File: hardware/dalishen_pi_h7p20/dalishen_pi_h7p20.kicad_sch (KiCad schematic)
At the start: 99 parts, among them J1 Conn_02x05_Odd_Even, J6 5V, J7 OV5640, J9 D500C930SV0, SW1 SW_Push, SW2 SW_Push, SW3 SW_DIP_x03, SW4 SW_Push, SW5 SW_Push, U3 H7P20N0L128-M3H1, U4 SY7201ABC, U5 XC6206-2.8, U7 P25Q64SH-SSH-IR, U8 XC6206-1.5, X1 NC

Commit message: [dalishen_pi_h7p20] 68013替换为双USB3343
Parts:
- removed C2: NC, Capacitor_SMD:C_0402_1005Metric, symbol Device:C
- removed CY_J1, CY_J2: Conn_02x10_Odd_Even, Connector_PinSocket_2.54mm:PinSocket_2x10_P2.54mm_Vertical, symbol Connector_Generic:Conn_02x10_Odd_Even
- removed J6: 5V, Connector_PinSocket_2.54mm:PinSocket_1x01_P2.54mm_Vertical, symbol Connector_Generic:Conn_01x01
- removed JP1: SolderJumper_2_Open, Jumper:SolderJumper-2_P1.3mm_Open_RoundedPad1.0x1.5mm, symbol Jumper:SolderJumper_2_Open
- removed R16: 2.49k, Resistor_SMD:R_0402_1005Metric, symbol Device:R
- removed R7: NC, Resistor_SMD:R_0402_1005Metric, symbol Device:R
- removed R8: 33, Resistor_SMD:R_0402_1005Metric, symbol Device:R
- removed X1: NC, vllogic:OSC_3225, symbol Oscillator:XO32
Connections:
- net LED_PWM: no longer U3.8 (IO17_8)
- net USB334x_SP1_D4: now reaches U3.6 (IO13_PCLK_8)
- net CY_FD_0 renamed USB334x_SP1_STP
- net CY_FD_1 renamed USB334x_SP1_DIR
- net CY_FD_10 renamed USB334x_SP2_CLK
- net CY_FD_11 renamed USB334x_SP1_26M
- net CY_FD_12 renamed USB334x_SP1_NXT
- net CY_FD_13 renamed USB334x_SP1_CLK
- net CY_FD_14 renamed USB334x_SP1_D0
- net CY_FD_15 renamed USB334x_SP1_D1
- net CY_FD_2 renamed USB334x_SP1_D7
- net CY_FD_3 renamed USB334x_SP1_D6
- net CY_FD_4 renamed USB334x_SP2_26M
- net CY_FD_5 renamed USB334x_SP2_NXT
- net CY_FD_6 renamed USB334x_SP2_STP
- net CY_FD_7 renamed USB334x_SP2_DIR
- net CY_FD_8 renamed USB334x_SP2_D1
- net CY_FD_9 renamed USB334x_SP2_D0
- net CY_FLAGB renamed USB334x_SP2_D7
- net CY_IFCLK renamed USB334x_SP1_D3
- net CY_PA0 renamed USB334x_SP2_D5
- net CY_PA1 renamed USB334x_SP2_D4
- net CY_PA3 renamed USB334x_SP2_D3
- net CY_PKTEND renamed USB334x_SP2_D2
- net CY_SLRD renamed USB334x_SP2_D6
- net CY_SLWR renamed USB334x_SP1_D2
- new net USB334x_SP1_D5: U3.8 (IO17_8)
- no-connect marks 16 -> 12
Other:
- added sheet USB334x_SP1 (USB334x_SP.kicad_sch)
- added sheet USB334x_SP2 (USB334x_SP.kicad_sch)
- sheet USB334x ports: added none; removed USB20_DM_CMP1, USB20_DM_CMP2, USB20_DM_CMP3, USB20_DP_CMP1, USB20_DP_CMP2, USB20_DP_CMP3
- note removed: "EZ-USB CY7C68013A板 对接口（顶对顶） 若68013板已焊排针，本板需焊双排母对接"
- note removed: "PD3 PD1 PA7 PA5 PA3 PA1 CTL2 CTL0 PB6 PB4"
- note removed: "PD4 PD2 PD0 PA6 PA4 PA2 PA0 CTL1 PB7 PB5"
- note removed: "PD5 PD7 CLK RDY0 GND GND SCL PB0 PB2 GND"
- note removed: "PD6 GND GND RDY1 VCC IFCLK SDA PB1 PB3 VCC"
- note removed: "注：JP1短接后可对外输出3.3V。对接EZ-USB板时不要短接。"
- moved on the sheet: C10, C11, C16, C17, C18, C19, C20, C21, C22, C23, C24, C38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

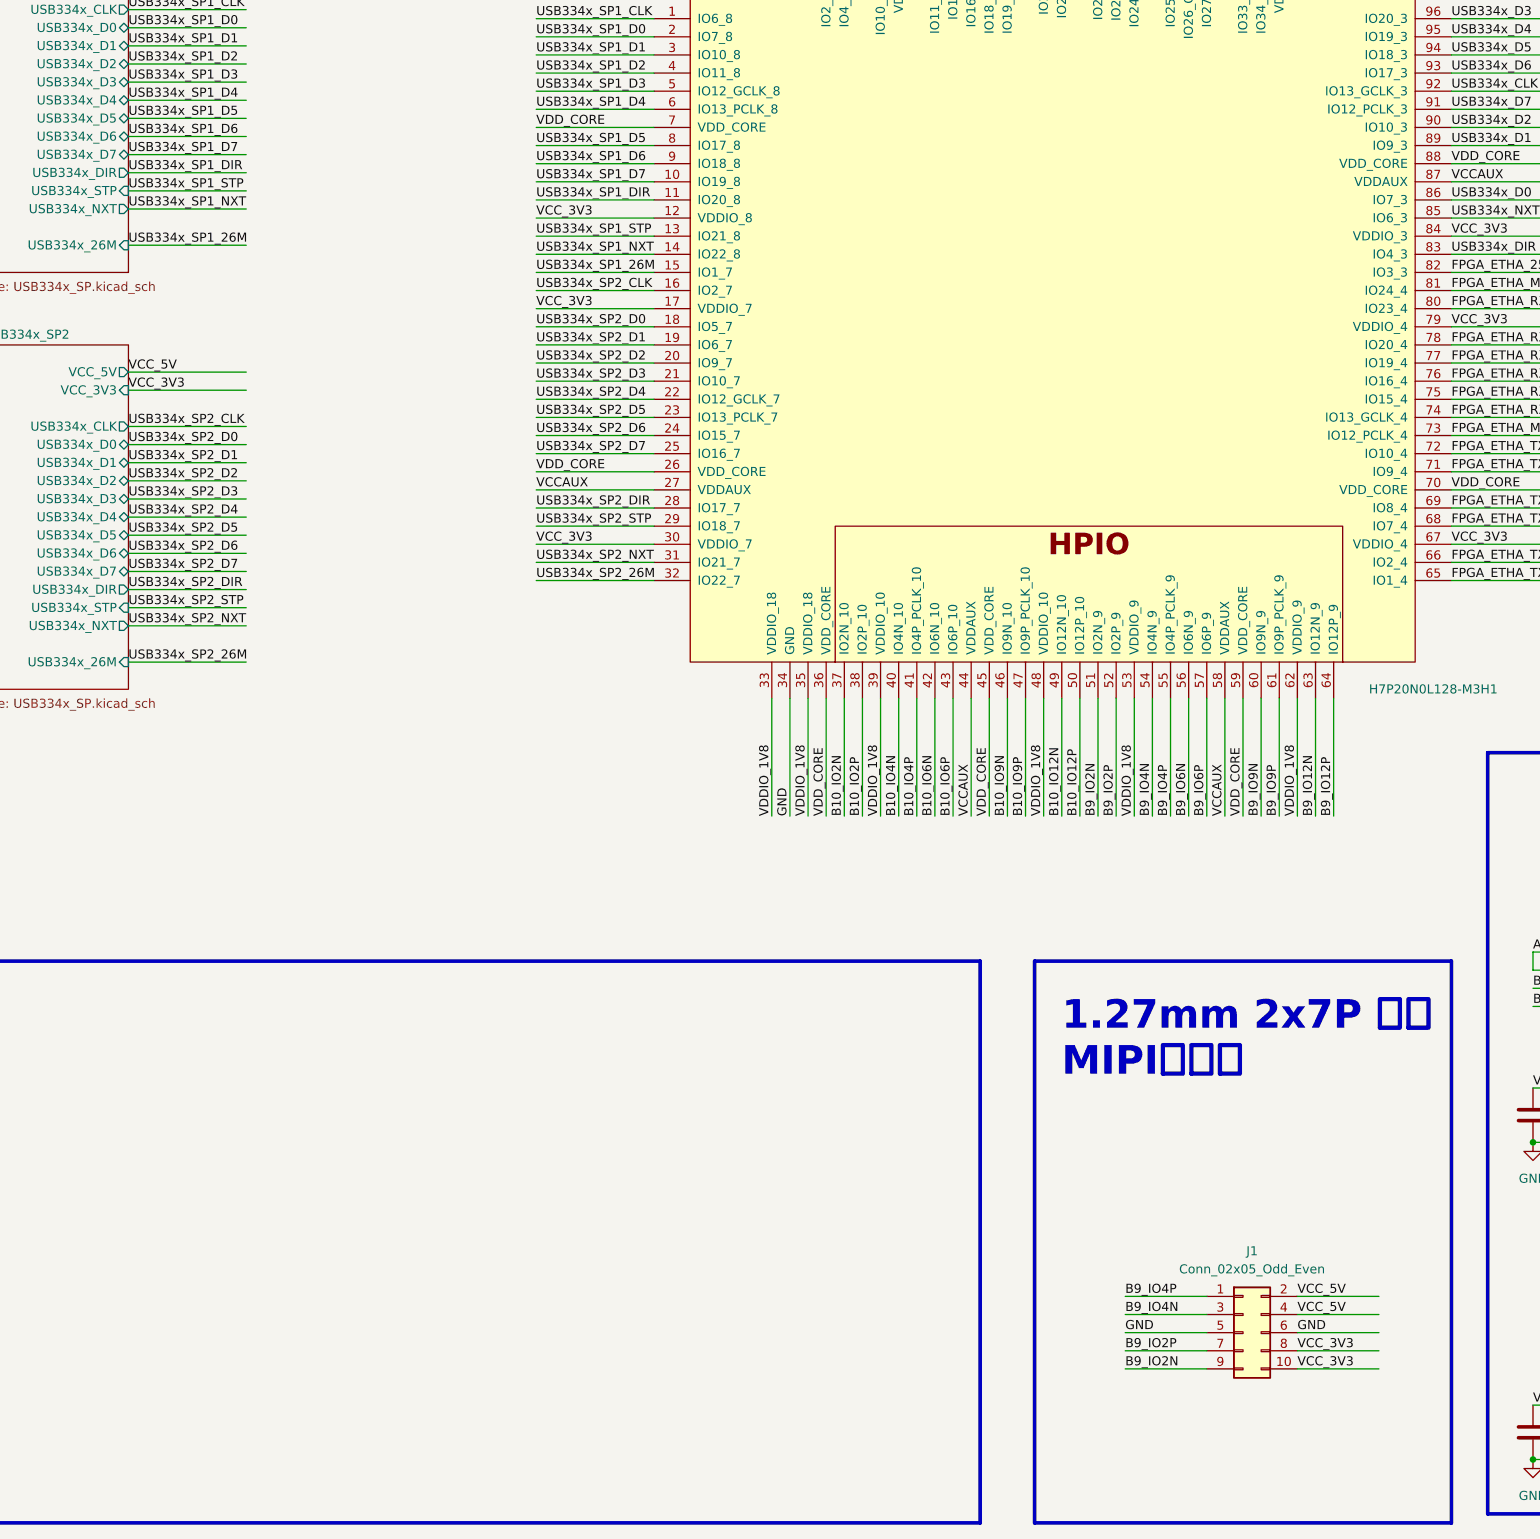
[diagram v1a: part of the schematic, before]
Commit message: [dalishen_pi_h7p20] 增加I2C小屏，增加两个测试IO
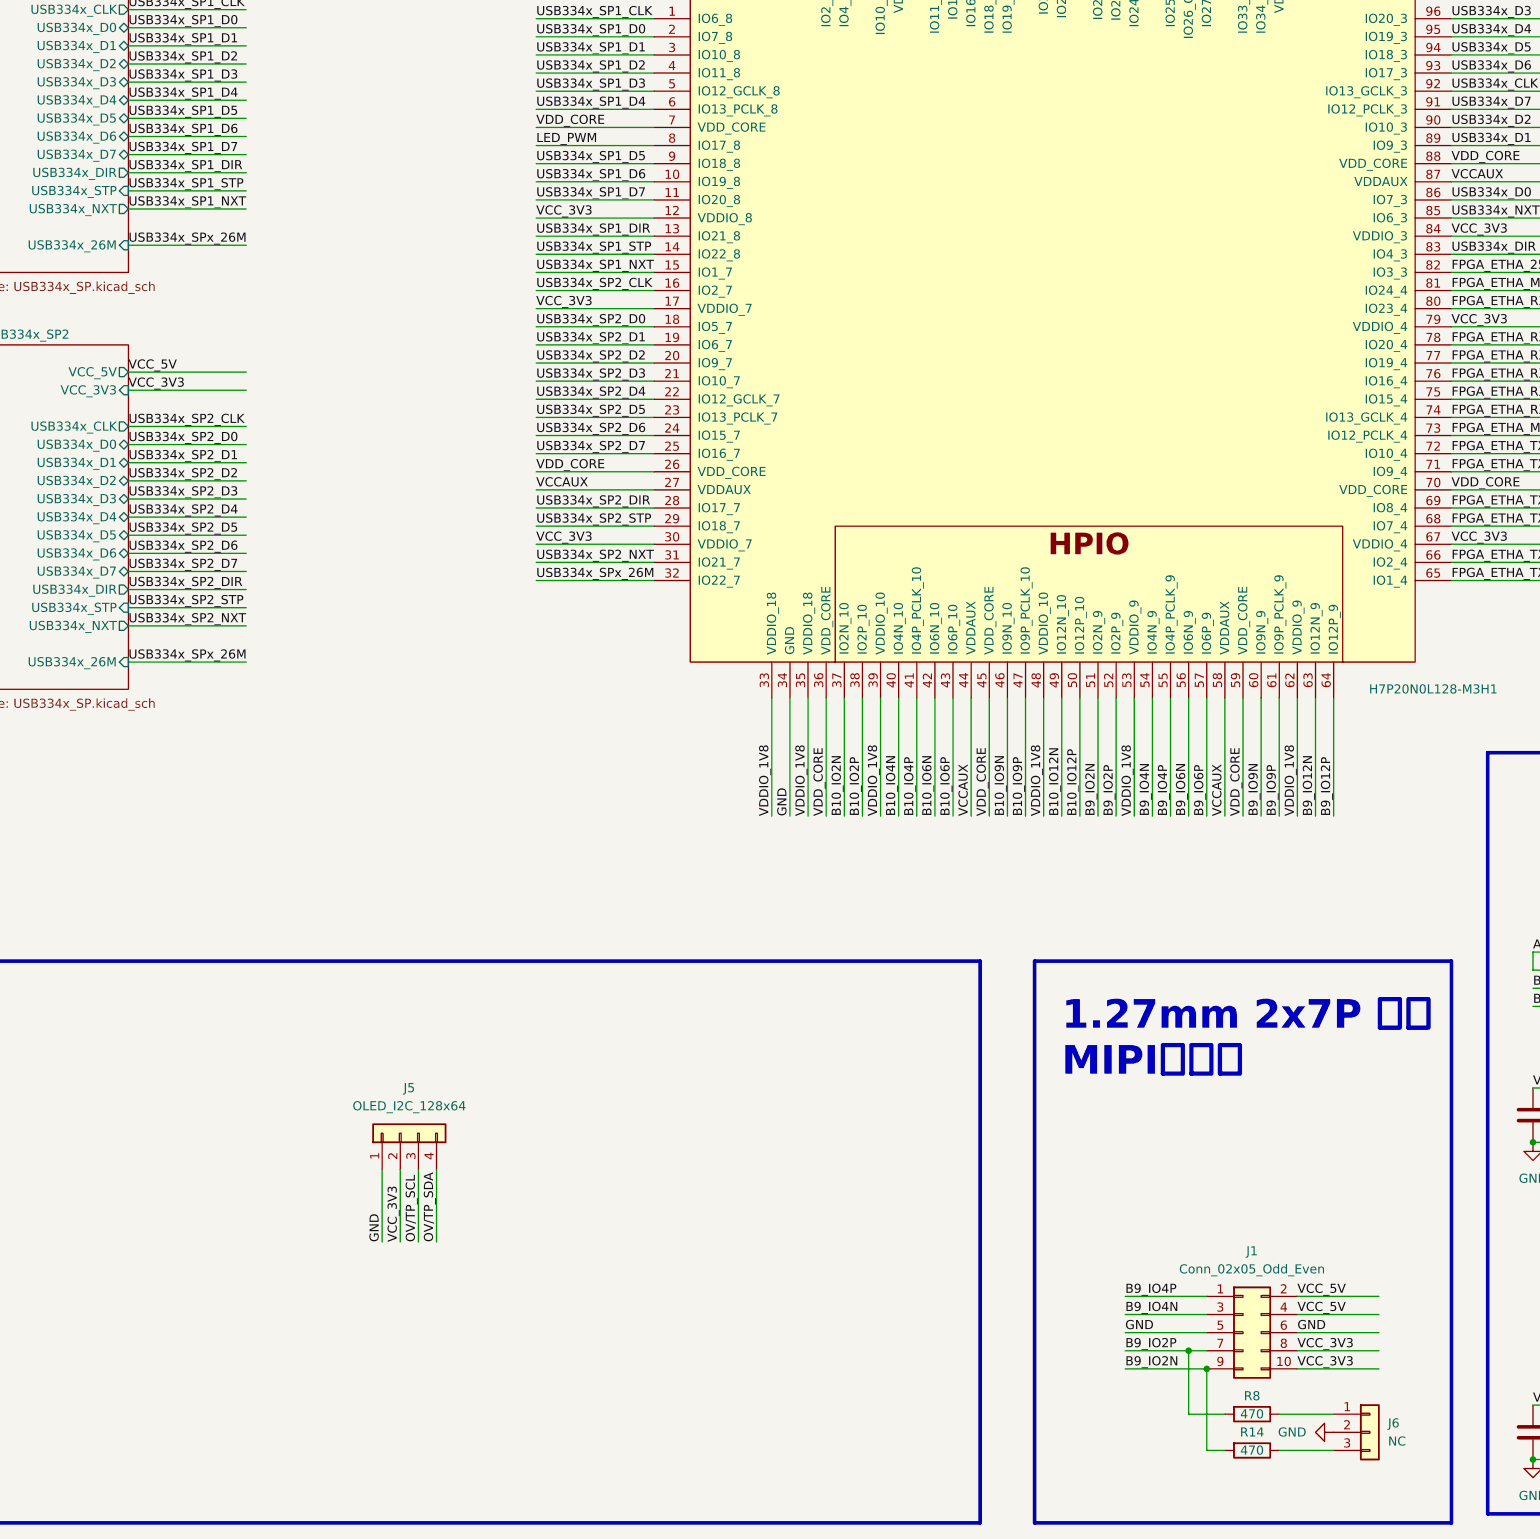
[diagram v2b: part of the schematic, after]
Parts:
- added J5: OLED_I2C_128x64, symbol Connector_Generic:Conn_01x04
- added J6: NC, symbol Connector_Generic:Conn_01x03
- added R14, R8: 470, Resistor_SMD:R_0402_1005Metric, symbol Device:R
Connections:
- net USB334x_SP1_26M is gone; now on net USB334x_SP1_NXT: U3.15 (IO1_7)
- net B9_IO2N: now also R14.2
- net B9_IO2P: now also R8.2
- net GND: now also J5.1 (Pin_1), J6.2 (Pin_2)
- net LED_PWM: now also U3.8 (IO17_8)
- net OV/TP_SCL: now also J5.3 (Pin_3)
- net OV/TP_SDA: now also J5.4 (Pin_4)
- net USB334x_SP1_D5: now also U3.9 (IO18_8); no longer U3.8 (IO17_8)
- net USB334x_SP1_D6: now also U3.10 (IO19_8); no longer U3.9 (IO18_8)
- net USB334x_SP1_D7: now also U3.11 (IO20_8); no longer U3.10 (IO19_8)
- net USB334x_SP1_DIR: now also U3.13 (IO21_8); no longer U3.11 (IO20_8)
- net USB334x_SP1_NXT: no longer U3.14 (IO22_8)
- net USB334x_SP1_STP: now also U3.14 (IO22_8); no longer U3.13 (IO21_8)
- net VCC_3V3: now also J5.2 (Pin_2)
- net USB334x_SP2_26M renamed USB334x_SPx_26M
- new net: J6.1 (Pin_1), R8.1
- new net: J6.3 (Pin_3), R14.1

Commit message: [dalishen_pi_h7p20] Backup
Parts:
- added FID1, FID2, FID3: Fiducial, Fiducial:Fiducial_1mm_Mask2mm, symbol Mechanical:Fiducial
- added R10, R24: 33, Resistor_SMD:R_0402_1005Metric, symbol Device:R
- J5: footprint (none) -> Connector_PinSocket_2.54mm:PinSocket_1x04_P2.54mm_Vertical
- J6: footprint (none) -> Connector_PinHeader_2.54mm:PinHeader_1x03_P2.54mm_Vertical
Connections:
- net USB334x_SPx_26M: now also R10.1, R24.1
- new net USB334x_SP1/USB334x_26M: R24.2
- new net USB334x_SP2/USB334x_26M: R10.2

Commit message: [dalishen_pi_h7p20] Backup
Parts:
- J6: footprint Connector_PinHeader_2.54mm:PinHeader_1x03_P2.54mm_Vertical -> Connector_PinHeader_2.54mm:PinHeader_1x03_P2.54mm_Horizontal
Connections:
- net KEY0 is gone; now on net KEY1: SW1.1, U3.126 (IO3_8)
- net KEY1: no longer SW4.1, U3.104 (IO27_GCLK_2)
- net KEY2: now also SW4.1, U3.104 (IO27_GCLK_2); no longer SW5.1, U3.102 (IO33_MISO3_2)
- net USB334x_SP1_CLK: now also U3.5 (IO12_GCLK_8); no longer U3.1 (IO6_8)
- net USB334x_SP1_D0: now also U3.3 (IO10_8); no longer U3.2 (IO7_8)
- net USB334x_SP1_D1: now also U3.2 (IO7_8); no longer U3.3 (IO10_8)
- net USB334x_SP1_D2: now also U3.1 (IO6_8); no longer U3.4 (IO11_8)
- net USB334x_SP1_D3: now also U3.13 (IO21_8); no longer U3.5 (IO12_GCLK_8)
- net USB334x_SP1_D4: now also U3.11 (IO20_8); no longer U3.6 (IO13_PCLK_8)
- net USB334x_SP1_D5: now also U3.10 (IO19_8); no longer U3.9 (IO18_8)
- net USB334x_SP1_D6: now also U3.9 (IO18_8); no longer U3.10 (IO19_8)
- net USB334x_SP1_D7: now also U3.6 (IO13_PCLK_8); no longer U3.11 (IO20_8)
- net USB334x_SP1_DIR: now also U3.14 (IO22_8); no longer U3.13 (IO21_8)
- net USB334x_SP1_NXT: now also U3.4 (IO11_8); no longer U3.15 (IO1_7)
- net USB334x_SP1_STP: now also U3.15 (IO1_7); no longer U3.14 (IO22_8)
- net USB334x_SP2_CLK: now also U3.22 (IO12_GCLK_7); no longer U3.16 (IO2_7)
- net USB334x_SP2_D0: now also U3.20 (IO9_7); no longer U3.18 (IO5_7)
- net USB334x_SP2_D2: now also U3.18 (IO5_7); no longer U3.20 (IO9_7)
- net USB334x_SP2_D3: now also U3.29 (IO18_7); no longer U3.21 (IO10_7)
- net USB334x_SP2_D4: now also U3.28 (IO17_7); no longer U3.22 (IO12_GCLK_7)
- net USB334x_SP2_D5: now also U3.25 (IO16_7); no longer U3.23 (IO13_PCLK_7)
- net USB334x_SP2_D7: now also U3.23 (IO13_PCLK_7); no longer U3.25 (IO16_7)
- net USB334x_SP2_DIR: now also U3.31 (IO21_7); no longer U3.28 (IO17_7)
- net USB334x_SP2_NXT: now also U3.21 (IO10_7); no longer U3.31 (IO21_7)
- net USB334x_SP2_STP: now also U3.32 (IO22_7); no longer U3.29 (IO18_7)
- net USB334x_SPx_26M: now also U3.16 (IO2_7); no longer U3.32 (IO22_7)
- new net KEY3: SW5.1, U3.102 (IO33_MISO3_2)
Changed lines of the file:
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@@
 		)
 	)
-	(label "KEY1"
+	(label "KEY2"
 		(at 189.23 54.61 90)
 		(effects
@@
 	)
 	(label "USB334x_SP2_D4"
-		(at 95.25 124.46 0)
+		(at 95.25 139.7 0)
 		(effects
 			(font
@@
 	)
 	(label "USB334x_SP1_D0"
-		(at 95.25 73.66 0)
+		(at 95.25 76.2 0)
 		(effects
 			(font
@@
 	)
 	(label "USB334x_SP1_D6"
-		(at 95.25 93.98 0)
+		(at 95.25 91.44 0)
 		(effects
 			(font
@@
 	)
 	(label "USB334x_SP1_D5"
-		(at 95.25 91.44 0)
+		(at 95.25 93.98 0)
 		(effects
 			(font
@@
 	)
 	(label "USB334x_SP1_D7"
-		(at 95.25 96.52 0)
+		(at 95.25 83.82 0)
 		(effects
 			(font
@@
 	)
 	(label "USB334x_SP2_D5"
-		(at 95.25 127 0)
+		(at 95.25 132.08 0)
 		(effects
 			(font
@@
 	)
 	(label "USB334x_SP1_D1"
-		(at 95.25 76.2 0)
+		(at 95.25 73.66 0)
 		(effects
 			(font
@@
 	)
 	(label "USB334x_SP1_D4"
-		(at 95.25 83.82 0)
+		(at 95.25 96.52 0)
 		(effects
 			(font
@@
 		)
 	)
-	(label "KEY0"
+	(label "KEY1"
 		(at 133.35 54.61 90)
 		(effects
@@
 		)
 	)
-	(label "KEY2"
+	(label "KEY3"
 		(at 264.16 88.9 0)
 		(effects
@@
 		)
 	)
-	(label "KEY2"
+	(label "KEY3"
 		(at 194.31 54.61 90)
 		(effects
@@
 	)
 	(label "USB334x_SP1_NXT"
-		(at 95.25 106.68 0)
+		(at 95.25 78.74 0)
 		(effects
 			(font
@@
 	)
 	(label "USB334x_SP1_STP"
-		(at 95.25 104.14 0)
+		(at 95.25 106.68 0)
 		(effects
 			(font
@@
 		)
 	)
-	(label "KEY1"
+	(label "KEY2"
 		(at 264.16 83.82 0)
 		(effects
@@
 	)
 	(label "USB334x_SP1_D2"
-		(at 95.25 78.74 0)
+		(at 95.25 71.12 0)
 		(effects
 			(font
@@
 	)
 	(label "USB334x_SP2_D0"
-		(at 95.25 114.3 0)
+		(at 95.25 119.38 0)
 		(effects
 			(font
@@
 	)
 	(label "USB334x_SP2_D3"
-		(at 95.25 121.92 0)
+		(at 95.25 142.24 0)
 		(effects
 			(font
@@
 	)
 	(label "USB334x_SP2_D2"
-		(at 95.25 119.38 0)
+		(at 95.25 114.3 0)
 		(effects
 			(font
@@
 	)
 	(label "USB334x_SP2_DIR"
-		(at 95.25 139.7 0)
+		(at 95.25 147.32 0)
 		(effects
 			(font
@@
 	)
 	(label "USB334x_SP1_CLK"
-		(at 95.25 71.12 0)
+		(at 95.25 81.28 0)
 		(effects
 			(font
@@
 	)
 	(label "USB334x_SP2_CLK"
-		(at 95.25 109.22 0)
+		(at 95.25 124.46 0)
 		(effects
 			(font
@@
 	)
 	(label "USB334x_SP2_D7"
-		(at 95.25 132.08 0)
+		(at 95.25 127 0)
 		(effects
 			(font
@@
 		)
 	)
-	(label "KEY0"
+	(label "KEY1"
 		(at 264.16 78.74 0)
 		(effects
@@
 	)
 	(label "USB334x_SP1_D3"
-		(at 95.25 81.28 0)
+		(at 95.25 101.6 0)
 		(effects
 			(font
@@
 	)
 	(label "USB334x_SP2_STP"
-		(at 95.25 142.24 0)
+		(at 95.25 149.86 0)
 		(effects
 			(font
@@
 	)
 	(label "USB334x_SPx_26M"
-		(at 95.25 149.86 0)
+		(at 95.25 109.22 0)
 		(effects
 			(font
@@
 	)
 	(label "USB334x_SP2_NXT"
-		(at 95.25 147.32 0)
+		(at 95.25 121.92 0)
 		(effects
 			(font
@@
 	)
 	(label "USB334x_SP1_DIR"
-		(at 95.25 101.6 0)
+		(at 95.25 104.14 0)
 		(effects
 			(font
@@
 			)
 		)
-		(property "Footprint" "Connector_PinHeader_2.54mm:PinHeader_1x03_P2.54mm_Vertical"
+		(property "Footprint" "Connector_PinHeader_2.54mm:PinHeader_1x03_P2.54mm_Horizontal"
 			(at 212.09 269.24 0)
 			(effects

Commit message: [dalishen_pi_h7p20] 待review
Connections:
- net USB334x_SP1_CLK renamed USB334x_SP1_C/R
- net USB334x_SP2_CLK renamed USB334x_SP2_C/R
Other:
- sheet USB334x_SP1 ports: added USB334x_C/R; removed USB334x_CLK
- sheet USB334x_SP2 ports: added USB334x_C/R; removed USB334x_CLK
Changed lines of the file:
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@@
 		)
 	)
-	(label "USB334x_SP2_CLK"
+	(label "USB334x_SP2_C{slash}R"
 		(at 38.1 128.27 0)
 		(effects
@@
 		)
 	)
-	(label "USB334x_SP1_CLK"
+	(label "USB334x_SP1_C{slash}R"
 		(at 38.1 69.85 0)
 		(effects
@@
 		)
 	)
-	(label "USB334x_SP1_CLK"
+	(label "USB334x_SP1_C{slash}R"
 		(at 95.25 81.28 0)
 		(effects
@@
 		)
 	)
-	(label "USB334x_SP2_CLK"
+	(label "USB334x_SP2_C{slash}R"
 		(at 95.25 124.46 0)
 		(effects
@@
 			)
 		)
-		(pin "USB334x_CLK" output
+		(pin "USB334x_C{slash}R" bidirectional
 			(at 38.1 69.85 0)
 			(effects
@@
 			)
 		)
-		(pin "USB334x_CLK" output
+		(pin "USB334x_C{slash}R" bidirectional
 			(at 38.1 128.27 0)
 			(effects

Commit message: [dalishen_pi_h7p20] 打样
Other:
- note added: "0.96寸 I2C OLED 屏幕模块接口"
- moved on the sheet: J5
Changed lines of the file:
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@@
 	)
 	(rectangle
-		(start 15.24 203.2)
+		(start 106.68 203.2)
 		(end 157.48 281.94)
 		(stroke
@@
 		)
 	)
+	(text "0.96寸 I2C OLED\n屏幕模块接口"
+		(exclude_from_sim no)
+		(at 108.585 220.345 0)
+		(effects
+			(font
+				(face "仿宋")
+				(size 4 4)
+				(thickness 0.6)
+				(bold yes)
+			)
+			(justify left bottom)
+		)
+	)
 	(junction
 		(at 248.92 21.59)
@@
 	(wire
 		(pts
-			(xy 73.66 232.41) (xy 73.66 242.57)
+			(xy 128.27 237.49) (xy 128.27 247.65)
 		)
 		(stroke
@@
 	(wire
 		(pts
-			(xy 78.74 232.41) (xy 78.74 242.57)
+			(xy 133.35 237.49) (xy 133.35 247.65)
 		)
 		(stroke
@@
 	(wire
 		(pts
-			(xy 76.2 232.41) (xy 76.2 242.57)
+			(xy 130.81 237.49) (xy 130.81 247.65)
 		)
 		(stroke
@@
 	(wire
 		(pts
-			(xy 81.28 232.41) (xy 81.28 242.57)
+			(xy 135.89 237.49) (xy 135.89 247.65)
 		)
 		(stroke
@@
 	)
 	(label "OV{slash}TP_SDA"
-		(at 81.28 242.57 90)
+		(at 135.89 247.65 90)
 		(effects
 			(font
@@
 	)
 	(label "OV{slash}TP_SCL"
-		(at 78.74 242.57 90)
+		(at 133.35 247.65 90)
 		(effects
 			(font
@@
 	)
 	(label "VCC_3V3"
-		(at 76.2 242.57 90)
+		(at 130.81 247.65 90)
 		(effects
 			(font
@@
 	)
 	(label "GND"
-		(at 73.66 242.57 90)
+		(at 128.27 247.65 90)
 		(effects
 			(font
@@
 	(symbol
 		(lib_id "Connector_Generic:Conn_01x04")
-		(at 76.2 227.33 90)
+		(at 130.81 232.41 90)
 		(unit 1)
 		(exclude_from_sim no)
@@
 		(fields_autoplaced yes)
 		(property "Reference" "J5"
-			(at 77.47 220.98 90)
+			(at 132.08 226.06 90)
 			(effects
 				(font
@@
 		)
 		(property "Value" "OLED_I2C_128x64"
-			(at 77.47 223.52 90)
+			(at 132.08 228.6 90)
 			(effects
 				(font
@@
 		)
 		(property "Footprint" "Connector_PinSocket_2.54mm:PinSocket_1x04_P2.54mm_Vertical"
-			(at 76.2 227.33 0)
+			(at 130.81 232.41 0)
 			(effects
 				(font
@@
 		)
 		(property "Datasheet" "~"
-			(at 76.2 227.33 0)
+			(at 130.81 232.41 0)
 			(effects
 				(font
@@
 		)
 		(property "Description" "Generic connector, single row, 01x04, script generated (kicad-library-utils/schlib/autogen/connector/)"
-			(at 76.2 227.33 0)
+			(at 130.81 232.41 0)
 			(effects
 				(font
